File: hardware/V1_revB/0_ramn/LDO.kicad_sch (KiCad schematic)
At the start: 4 parts

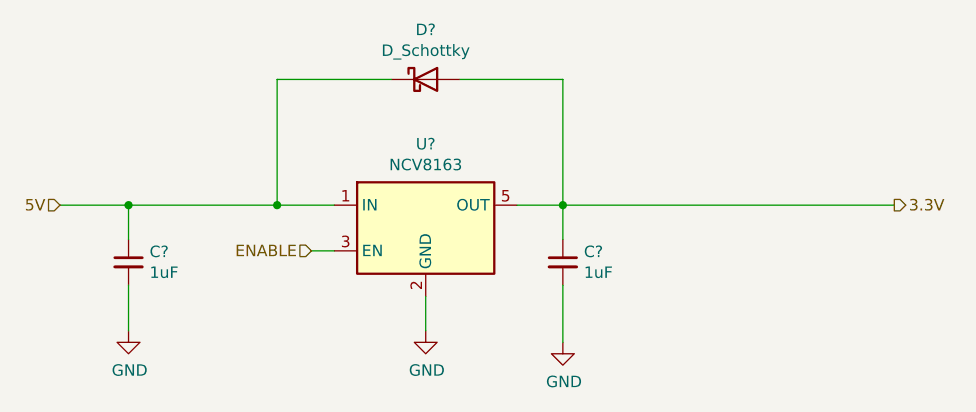
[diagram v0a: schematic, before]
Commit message: Feat(Hw):Modify_BOM_LCSC#
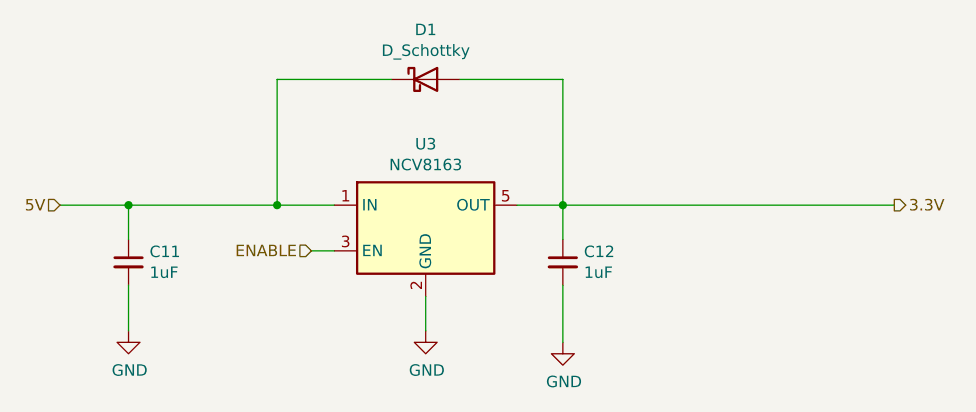
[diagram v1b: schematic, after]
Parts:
- C11, C12: renamed from C?; LCSC# (none) -> C90539
- D1: renamed from D?; LCSC# (none) -> C154821
- U3: renamed from U?; LCSC# (none) -> C604041

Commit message: Feat(Hw): UpdateKiCadProjectAndStandardizeComponentProperties
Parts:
- C11, C12: Category (none) -> Electronic Components / Capacitors; LCSC# C90539 -> (none); lcsc# (none) -> C90539; manf# (none) -> 1206B105K500NT
- D1: Category (none) -> Electronic Components / Diodes; LCSC# C154821 -> (none); lcsc# (none) -> C154821; manf# (none) -> RB520S30T1G
- U3: Category (none) -> Electronic Components / Integrated Circuits; LCSC# C604041 -> (none); lcsc# (none) -> C604041; manf# (none) -> NCV8163ASN330T1G
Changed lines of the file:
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@@
 			)
 		)
-		(property "LCSC#" "C604041"
-			(at 114.3 73.66 0)
-			(hide yes)
-			(show_name no)
-			(do_not_autoplace no)
-			(effects
-				(font
-					(size 1.27 1.27)
-				)
+		(property "manf#" "NCV8163ASN330T1G"
+			(at 0 0 0)
+			(effects
+				(font
+					(size 1.27 1.27)
+				)
+				(hide yes)
+			)
+		)
+		(property "lcsc#" "C604041"
+			(at 0 0 0)
+			(effects
+				(font
+					(size 1.27 1.27)
+				)
+				(hide yes)
+			)
+		)
+		(property "Category" "Electronic Components / Integrated Circuits"
+			(at 0 0 0)
+			(effects
+				(font
+					(size 1.27 1.27)
+				)
+				(hide yes)
 			)
 		)
@@
 			)
 		)
-		(property "LCSC#" "C90539"
-			(at 81.28 77.47 0)
-			(hide yes)
-			(show_name no)
-			(do_not_autoplace no)
-			(effects
-				(font
-					(size 1.27 1.27)
-				)
+		(property "manf#" "1206B105K500NT"
+			(at 0 0 0)
+			(effects
+				(font
+					(size 1.27 1.27)
+				)
+				(hide yes)
+			)
+		)
+		(property "lcsc#" "C90539"
+			(at 0 0 0)
+			(effects
+				(font
+					(size 1.27 1.27)
+				)
+				(hide yes)
+			)
+		)
+		(property "Category" "Electronic Components / Capacitors"
+			(at 0 0 0)
+			(effects
+				(font
+					(size 1.27 1.27)
+				)
+				(hide yes)
 			)
 		)
@@
 			)
 		)
-		(property "LCSC#" "C90539"
-			(at 129.54 77.47 0)
-			(hide yes)
-			(show_name no)
-			(do_not_autoplace no)
-			(effects
-				(font
-					(size 1.27 1.27)
-				)
+		(property "manf#" "1206B105K500NT"
+			(at 0 0 0)
+			(effects
+				(font
+					(size 1.27 1.27)
+				)
+				(hide yes)
+			)
+		)
+		(property "lcsc#" "C90539"
+			(at 0 0 0)
+			(effects
+				(font
+					(size 1.27 1.27)
+				)
+				(hide yes)
+			)
+		)
+		(property "Category" "Electronic Components / Capacitors"
+			(at 0 0 0)
+			(effects
+				(font
+					(size 1.27 1.27)
+				)
+				(hide yes)
 			)
 		)
@@
 			)
 		)
-		(property "LCSC#" "C154821"
-			(at 114.3 57.15 0)
-			(hide yes)
-			(show_name no)
-			(do_not_autoplace no)
-			(effects
-				(font
-					(size 1.27 1.27)
-				)
-			)
-		)
+		(property "manf#" "RB520S30T1G"
+			(at 0 0 0)
+			(effects
+				(font
+					(size 1.27 1.27)
+				)
+				(hide yes)
+			)
+		)
+		(property "lcsc#" "C154821"
+			(at 0 0 0)
+			(effects
+				(font
+					(size 1.27 1.27)
+				)
+				(hide yes)
+			)
+		)
+		(property "Category" "Electronic Components / Diodes"
+			(at 0 0 0)
+			(effects
+				(font
+					(size 1.27 1.27)
+				)
+				(hide yes)
+			)
+		)
